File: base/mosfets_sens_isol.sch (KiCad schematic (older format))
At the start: 72 parts, among them Q1 irf540n, Q2 irf540n, Q3 irf540n, Q4 irf540n, Q5 irf540n, Q6 irf540n, Q7 irf540n, Q8 irf540n, U1 SI8640, U10 ADS7886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

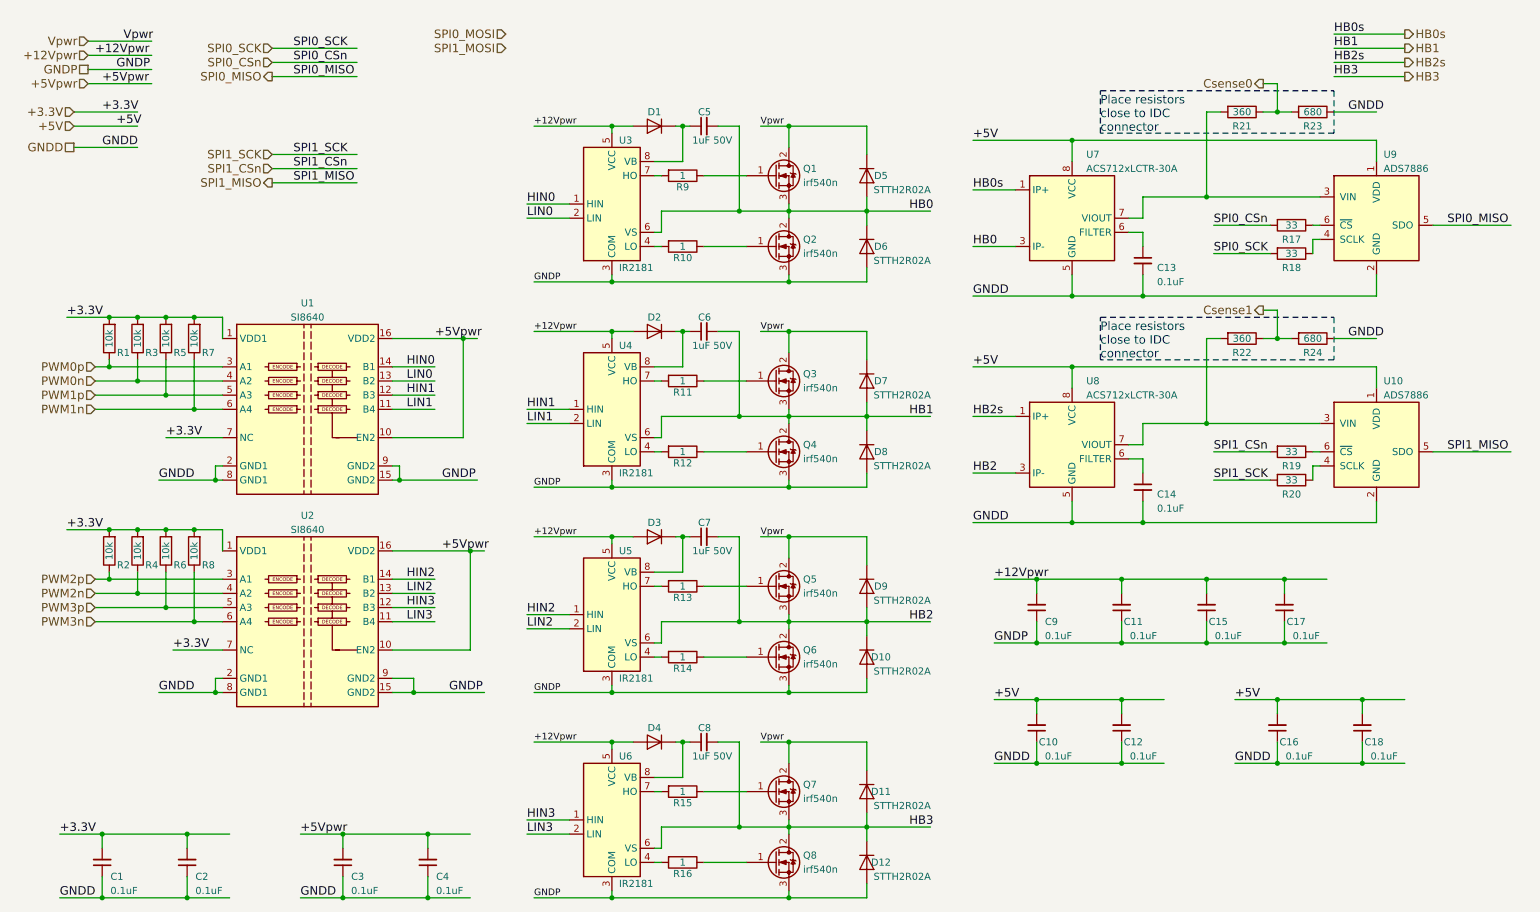
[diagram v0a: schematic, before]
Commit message: some test points
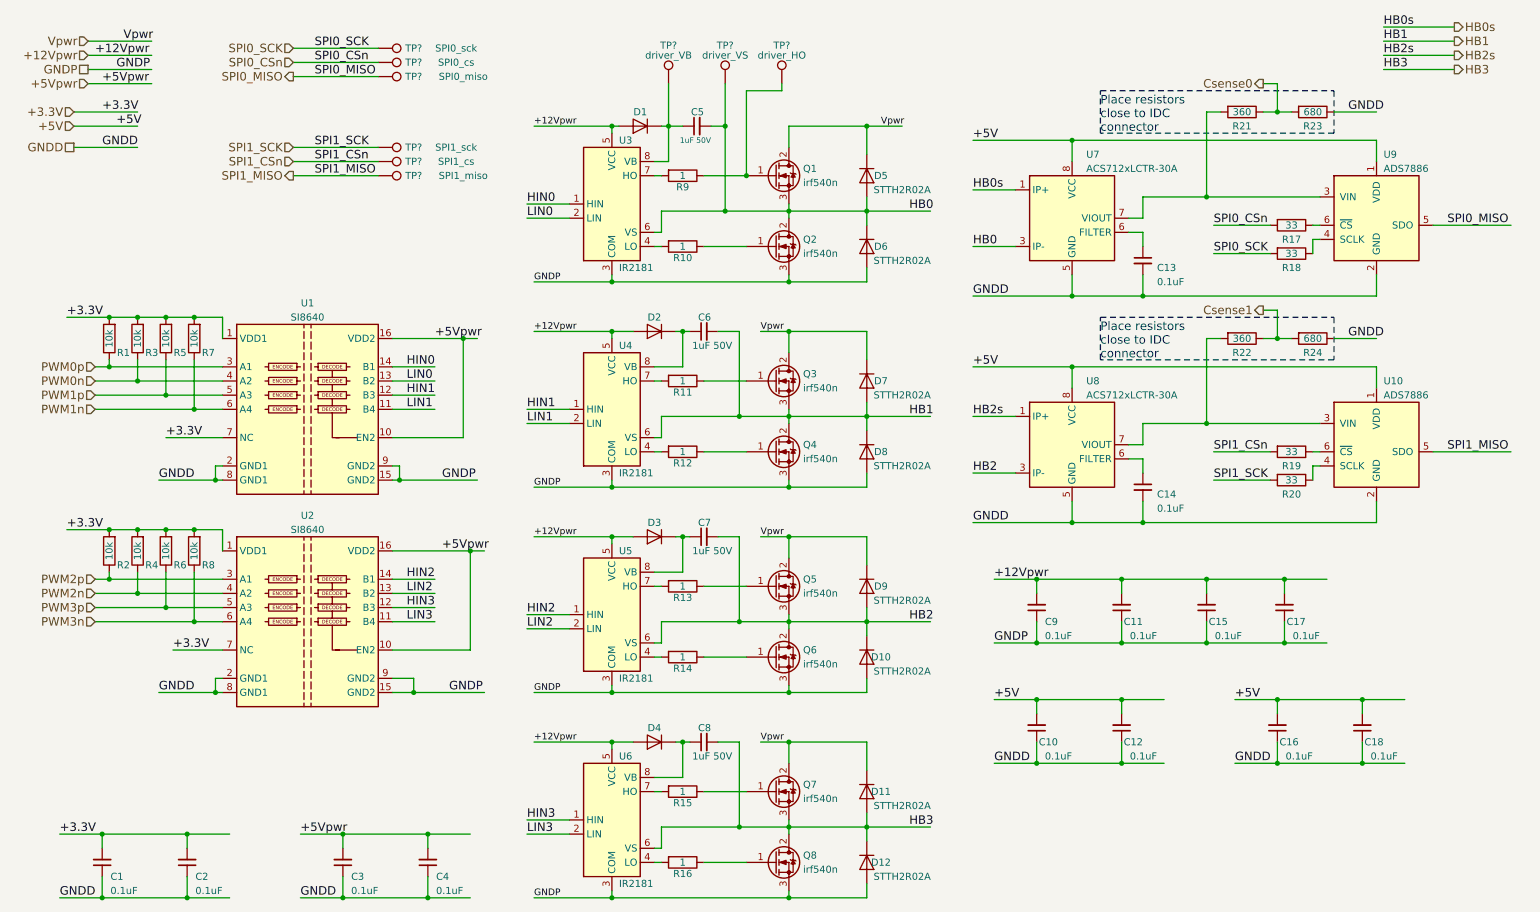
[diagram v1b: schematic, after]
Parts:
- added TP?: SPI0_sck, symbol Test_Point
- added TP?: SPI0_cs, symbol Test_Point
- added TP?: SPI0_miso, symbol Test_Point
- added TP?: SPI1_sck, symbol Test_Point
- added TP?: SPI1_cs, symbol Test_Point
- added TP?: SPI1_miso, symbol Test_Point
- added TP?: driver_VS, symbol Test_Point
- added TP?: driver_VB, symbol Test_Point
- added TP?: driver_HO, symbol Test_Point
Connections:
- net labels removed: SPI0_MOSI, SPI1_MOSI
- wire segments 251 -> 355
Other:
- moved on the sheet: C5, D1

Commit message: A few updates to test points.
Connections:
- wire segments 355 -> 254

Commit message: annotate sch
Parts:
- gave numbers to parts that had none: 9
- renumbered R21 to R17, R22 to R18, R17 to R19, R18 to R20, R19 to R21, R20 to R22
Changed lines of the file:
@@
 $EndComp
 $Comp
-L R R17
+L R R19
 U 1 1 5A3537D9
 P 9600 2000
-F 0 "R17" V 9700 2000 50  0000 C CNN
+F 0 "R19" V 9700 2000 50  0000 C CNN
 F 1 "33" V 9600 2000 50  0000 C CNN
 F 2 "Resistor_SMD:R_0603_1608Metric" H 9600 2000 50  0001 C CNN
@@
 $EndComp
 $Comp
-L R R18
+L R R20
 U 1 1 5A354104
 P 9600 2200
-F 0 "R18" V 9700 2200 50  0000 C CNN
+F 0 "R20" V 9700 2200 50  0000 C CNN
 F 1 "33" V 9600 2200 50  0000 C CNN
 F 2 "Resistor_SMD:R_0603_1608Metric" H 9600 2200 50  0001 C CNN
@@
 $EndComp
 $Comp
-L R R19
+L R R21
 U 1 1 5A35521E
 P 9600 3600
-F 0 "R19" V 9700 3600 50  0000 C CNN
+F 0 "R21" V 9700 3600 50  0000 C CNN
 F 1 "33" V 9600 3600 50  0000 C CNN
 F 2 "Resistor_SMD:R_0603_1608Metric" H 9600 3600 50  0001 C CNN
@@
 $EndComp
 $Comp
-L R R20
+L R R22
 U 1 1 5A35533D
 P 9600 3800
-F 0 "R20" V 9700 3800 50  0000 C CNN
+F 0 "R22" V 9700 3800 50  0000 C CNN
 F 1 "33" V 9600 3800 50  0000 C CNN
 F 2 "Resistor_SMD:R_0603_1608Metric" H 9600 3800 50  0001 C CNN
@@
 Csense1
 $Comp
-L R R21
+L R R17
 U 1 1 5A3EBCC5
 P 9250 1200
-F 0 "R21" V 9350 1200 50  0000 C CNN
+F 0 "R17" V 9350 1200 50  0000 C CNN
 F 1 "360" V 9250 1200 50  0000 C CNN
 F 2 "Resistor_SMD:R_0603_1608Metric" H 9250 1200 50  0001 C CNN
@@
 Place resistors\nclose to IDC\nconnector
 $Comp
-L R R22
+L R R18
 U 1 1 5A3EE220
 P 9250 2800
-F 0 "R22" V 9350 2800 50  0000 C CNN
+F 0 "R18" V 9350 2800 50  0000 C CNN
 F 1 "360" V 9250 2800 50  0000 C CNN
 F 2 "Resistor_SMD:R_0603_1608Metric" H 9250 2800 50  0001 C CNN
@@
 Place resistors\nclose to IDC\nconnector
 $Comp
-L Test_Point TP?
+L Test_Point TP21
 U 1 1 5A48CF04
 P 3150 750
-F 0 "TP?" V 3150 1000 50  0000 C CNN
+F 0 "TP21" V 3150 1000 50  0000 C CNN
 F 1 "SPI0_sck" V 3150 1300 50  0000 C CNN
 F 2 "" H 3350 750 50  0001 C CNN
@@
 $EndComp
 $Comp
-L Test_Point TP?
+L Test_Point TP22
 U 1 1 5A490640
 P 3150 850
-F 0 "TP?" V 3150 1100 50  0000 C CNN
+F 0 "TP22" V 3150 1100 50  0000 C CNN
 F 1 "SPI0_cs" V 3150 1400 50  0000 C CNN
 F 2 "" H 3350 850 50  0001 C CNN
@@
 $EndComp
 $Comp
-L Test_Point TP?
+L Test_Point TP23
 U 1 1 5A490983
 P 3150 950
-F 0 "TP?" V 3150 1200 50  0000 C CNN
+F 0 "TP23" V 3150 1200 50  0000 C CNN
 F 1 "SPI0_miso" V 3150 1550 50  0000 C CNN
 F 2 "" H 3350 950 50  0001 C CNN
@@
 $EndComp
 $Comp
-L Test_Point TP?
+L Test_Point TP24
 U 1 1 5A490FA0
 P 3150 1450
-F 0 "TP?" V 3150 1700 50  0000 C CNN
+F 0 "TP24" V 3150 1700 50  0000 C CNN
 F 1 "SPI1_sck" V 3150 2000 50  0000 C CNN
 F 2 "" H 3350 1450 50  0001 C CNN
@@
 $EndComp
 $Comp
-L Test_Point TP?
+L Test_Point TP25
 U 1 1 5A4910BE
 P 3150 1550
-F 0 "TP?" V 3150 1800 50  0000 C CNN
+F 0 "TP25" V 3150 1800 50  0000 C CNN
 F 1 "SPI1_cs" V 3150 2100 50  0000 C CNN
 F 2 "" H 3350 1550 50  0001 C CNN
@@
 $EndComp
 $Comp
-L Test_Point TP?
+L Test_Point TP26
 U 1 1 5A4911D3
 P 3150 1650
-F 0 "TP?" V 3150 1900 50  0000 C CNN
+F 0 "TP26" V 3150 1900 50  0000 C CNN
 F 1 "SPI1_miso" V 3150 2250 50  0000 C CNN
 F 2 "" H 3350 1650 50  0001 C CNN
@@
 $EndComp
 $Comp
-L Test_Point TP?
+L Test_Point TP28
 U 1 1 5A4A934F
 P 5600 1000
-F 0 "TP?" H 5600 1270 50  0000 C CNN
+F 0 "TP28" H 5600 1270 50  0000 C CNN
 F 1 "driver_VS" H 5600 1200 50  0000 C CNN
 F 2 "" H 5800 1000 50  0001 C CNN
@@
 $EndComp
 $Comp
-L Test_Point TP?
+L Test_Point TP27
 U 1 1 5A4A9424
 P 5200 1000
-F 0 "TP?" H 5200 1270 50  0000 C CNN
+F 0 "TP27" H 5200 1270 50  0000 C CNN
 F 1 "driver_VB" H 5200 1200 50  0000 C CNN
 F 2 "" H 5400 1000 50  0001 C CNN
@@
 $EndComp
 $Comp
-L Test_Point TP?
+L Test_Point TP29
 U 1 1 5A4AA2DB
 P 6000 1000
-F 0 "TP?" H 6000 1270 50  0000 C CNN
+F 0 "TP29" H 6000 1270 50  0000 C CNN
 F 1 "driver_HO" H 6000 1200 50  0000 C CNN
 F 2 "" H 6200 1000 50  0001 C CNN

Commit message: added footprints, created netlist
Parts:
- TP27, TP28, TP29: footprint (none) -> TestPoint:TestPoint_Pad_D1.5mm
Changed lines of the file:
@@
 F 0 "TP28" H 5600 1270 50  0000 C CNN
 F 1 "driver_VS" H 5600 1200 50  0000 C CNN
-F 2 "" H 5800 1000 50  0001 C CNN
+F 2 "TestPoint:TestPoint_Pad_D1.5mm" H 5800 1000 50  0001 C CNN
 F 3 "" H 5800 1000 50  0001 C CNN
 	1    5600 1000
@@
 F 0 "TP27" H 5200 1270 50  0000 C CNN
 F 1 "driver_VB" H 5200 1200 50  0000 C CNN
-F 2 "" H 5400 1000 50  0001 C CNN
+F 2 "TestPoint:TestPoint_Pad_D1.5mm" H 5400 1000 50  0001 C CNN
 F 3 "" H 5400 1000 50  0001 C CNN
 	1    5200 1000
@@
 F 0 "TP29" H 6000 1270 50  0000 C CNN
 F 1 "driver_HO" H 6000 1200 50  0000 C CNN
-F 2 "" H 6200 1000 50  0001 C CNN
+F 2 "TestPoint:TestPoint_Pad_D1.5mm" H 6200 1000 50  0001 C CNN
 F 3 "" H 6200 1000 50  0001 C CNN
 	1    6000 1000

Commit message: assign footprints
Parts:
- TP21, TP22, TP23, TP24, TP25, TP26: footprint (none) -> TestPoint:TestPoint_Pad_D1.5mm
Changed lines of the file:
@@
 F 0 "TP21" V 3150 1000 50  0000 C CNN
 F 1 "SPI0_sck" V 3150 1300 50  0000 C CNN
-F 2 "" H 3350 750 50  0001 C CNN
+F 2 "TestPoint:TestPoint_Pad_D1.5mm" H 3350 750 50  0001 C CNN
 F 3 "" H 3350 750 50  0001 C CNN
 	1    3150 750
@@
 F 0 "TP22" V 3150 1100 50  0000 C CNN
 F 1 "SPI0_cs" V 3150 1400 50  0000 C CNN
-F 2 "" H 3350 850 50  0001 C CNN
+F 2 "TestPoint:TestPoint_Pad_D1.5mm" H 3350 850 50  0001 C CNN
 F 3 "" H 3350 850 50  0001 C CNN
 	1    3150 850
@@
 F 0 "TP23" V 3150 1200 50  0000 C CNN
 F 1 "SPI0_miso" V 3150 1550 50  0000 C CNN
-F 2 "" H 3350 950 50  0001 C CNN
+F 2 "TestPoint:TestPoint_Pad_D1.5mm" H 3350 950 50  0001 C CNN
 F 3 "" H 3350 950 50  0001 C CNN
 	1    3150 950
@@
 F 0 "TP24" V 3150 1700 50  0000 C CNN
 F 1 "SPI1_sck" V 3150 2000 50  0000 C CNN
-F 2 "" H 3350 1450 50  0001 C CNN
+F 2 "TestPoint:TestPoint_Pad_D1.5mm" H 3350 1450 50  0001 C CNN
 F 3 "" H 3350 1450 50  0001 C CNN
 	1    3150 1450
@@
 F 0 "TP25" V 3150 1800 50  0000 C CNN
 F 1 "SPI1_cs" V 3150 2100 50  0000 C CNN
-F 2 "" H 3350 1550 50  0001 C CNN
+F 2 "TestPoint:TestPoint_Pad_D1.5mm" H 3350 1550 50  0001 C CNN
 F 3 "" H 3350 1550 50  0001 C CNN
 	1    3150 1550
@@
 F 0 "TP26" V 3150 1900 50  0000 C CNN
 F 1 "SPI1_miso" V 3150 2250 50  0000 C CNN
-F 2 "" H 3350 1650 50  0001 C CNN
+F 2 "TestPoint:TestPoint_Pad_D1.5mm" H 3350 1650 50  0001 C CNN
 F 3 "" H 3350 1650 50  0001 C CNN
 	1    3150 1650

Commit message: update fooprints for mosfet
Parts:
- Q1: footprint Package_TO_SOT_THT:TO-220-3_Horizontal -> Package_TO_SOT_THT:TO-220-3_TabUp
- Q2, Q3, Q4, Q5, Q6, Q7, Q8: footprint Package_TO_SOT_THT:TO-220-3_Vertical -> Package_TO_SOT_THT:TO-220-3_TabUp
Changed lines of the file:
@@
 F 0 "Q1" H 6150 1700 50  0000 L CNN
 F 1 "irf540n" H 6150 1600 50  0000 L CNN
-F 2 "Package_TO_SOT_THT:TO-220-3_Horizontal" H 6150 1750 50  0001 C CNN
+F 2 "Package_TO_SOT_THT:TO-220-3_TabUp" H 6150 1750 50  0001 C CNN
 F 3 "" H 5950 1650 50  0001 C CNN
 	1    5950 1650
@@
 F 0 "Q2" H 6150 2200 50  0000 L CNN
 F 1 "irf540n" H 6150 2100 50  0000 L CNN
-F 2 "Package_TO_SOT_THT:TO-220-3_Vertical" H 6150 2250 50  0001 C CNN
+F 2 "Package_TO_SOT_THT:TO-220-3_TabUp" H 6150 2250 50  0001 C CNN
 F 3 "" H 5950 2150 50  0001 C CNN
 	1    5950 2150
@@
 F 0 "Q3" H 6150 3150 50  0000 L CNN
 F 1 "irf540n" H 6150 3050 50  0000 L CNN
-F 2 "Package_TO_SOT_THT:TO-220-3_Vertical" H 6150 3200 50  0001 C CNN
+F 2 "Package_TO_SOT_THT:TO-220-3_TabUp" H 6150 3200 50  0001 C CNN
 F 3 "" H 5950 3100 50  0001 C CNN
 	1    5950 3100
@@
 F 0 "Q4" H 6150 3650 50  0000 L CNN
 F 1 "irf540n" H 6150 3550 50  0000 L CNN
-F 2 "Package_TO_SOT_THT:TO-220-3_Vertical" H 6150 3700 50  0001 C CNN
+F 2 "Package_TO_SOT_THT:TO-220-3_TabUp" H 6150 3700 50  0001 C CNN
 F 3 "" H 5950 3600 50  0001 C CNN
 	1    5950 3600
@@
 F 0 "Q5" H 6150 4600 50  0000 L CNN
 F 1 "irf540n" H 6150 4500 50  0000 L CNN
-F 2 "Package_TO_SOT_THT:TO-220-3_Vertical" H 6150 4650 50  0001 C CNN
+F 2 "Package_TO_SOT_THT:TO-220-3_TabUp" H 6150 4650 50  0001 C CNN
 F 3 "" H 5950 4550 50  0001 C CNN
 	1    5950 4550
@@
 F 0 "Q6" H 6150 5100 50  0000 L CNN
 F 1 "irf540n" H 6150 5000 50  0000 L CNN
-F 2 "Package_TO_SOT_THT:TO-220-3_Vertical" H 6150 5150 50  0001 C CNN
+F 2 "Package_TO_SOT_THT:TO-220-3_TabUp" H 6150 5150 50  0001 C CNN
 F 3 "" H 5950 5050 50  0001 C CNN
 	1    5950 5050
@@
 F 0 "Q7" H 6150 6050 50  0000 L CNN
 F 1 "irf540n" H 6150 5950 50  0000 L CNN
-F 2 "Package_TO_SOT_THT:TO-220-3_Vertical" H 6150 6100 50  0001 C CNN
+F 2 "Package_TO_SOT_THT:TO-220-3_TabUp" H 6150 6100 50  0001 C CNN
 F 3 "" H 5950 6000 50  0001 C CNN
 	1    5950 6000
@@
 F 0 "Q8" H 6150 6550 50  0000 L CNN
 F 1 "irf540n" H 6150 6450 50  0000 L CNN
-F 2 "Package_TO_SOT_THT:TO-220-3_Vertical" H 6150 6600 50  0001 C CNN
+F 2 "Package_TO_SOT_THT:TO-220-3_TabUp" H 6150 6600 50  0001 C CNN
 F 3 "" H 5950 6500 50  0001 C CNN
 	1    5950 6500
